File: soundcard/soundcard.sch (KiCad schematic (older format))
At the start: 32 parts, among them U1 74LS590, U10 74HC164, U11 74HC164, U12 74LS86, U2 74LS590, U3 74LS688, U4 74LS109, U5 74LS373, U6 74LS373, U8 74LS138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

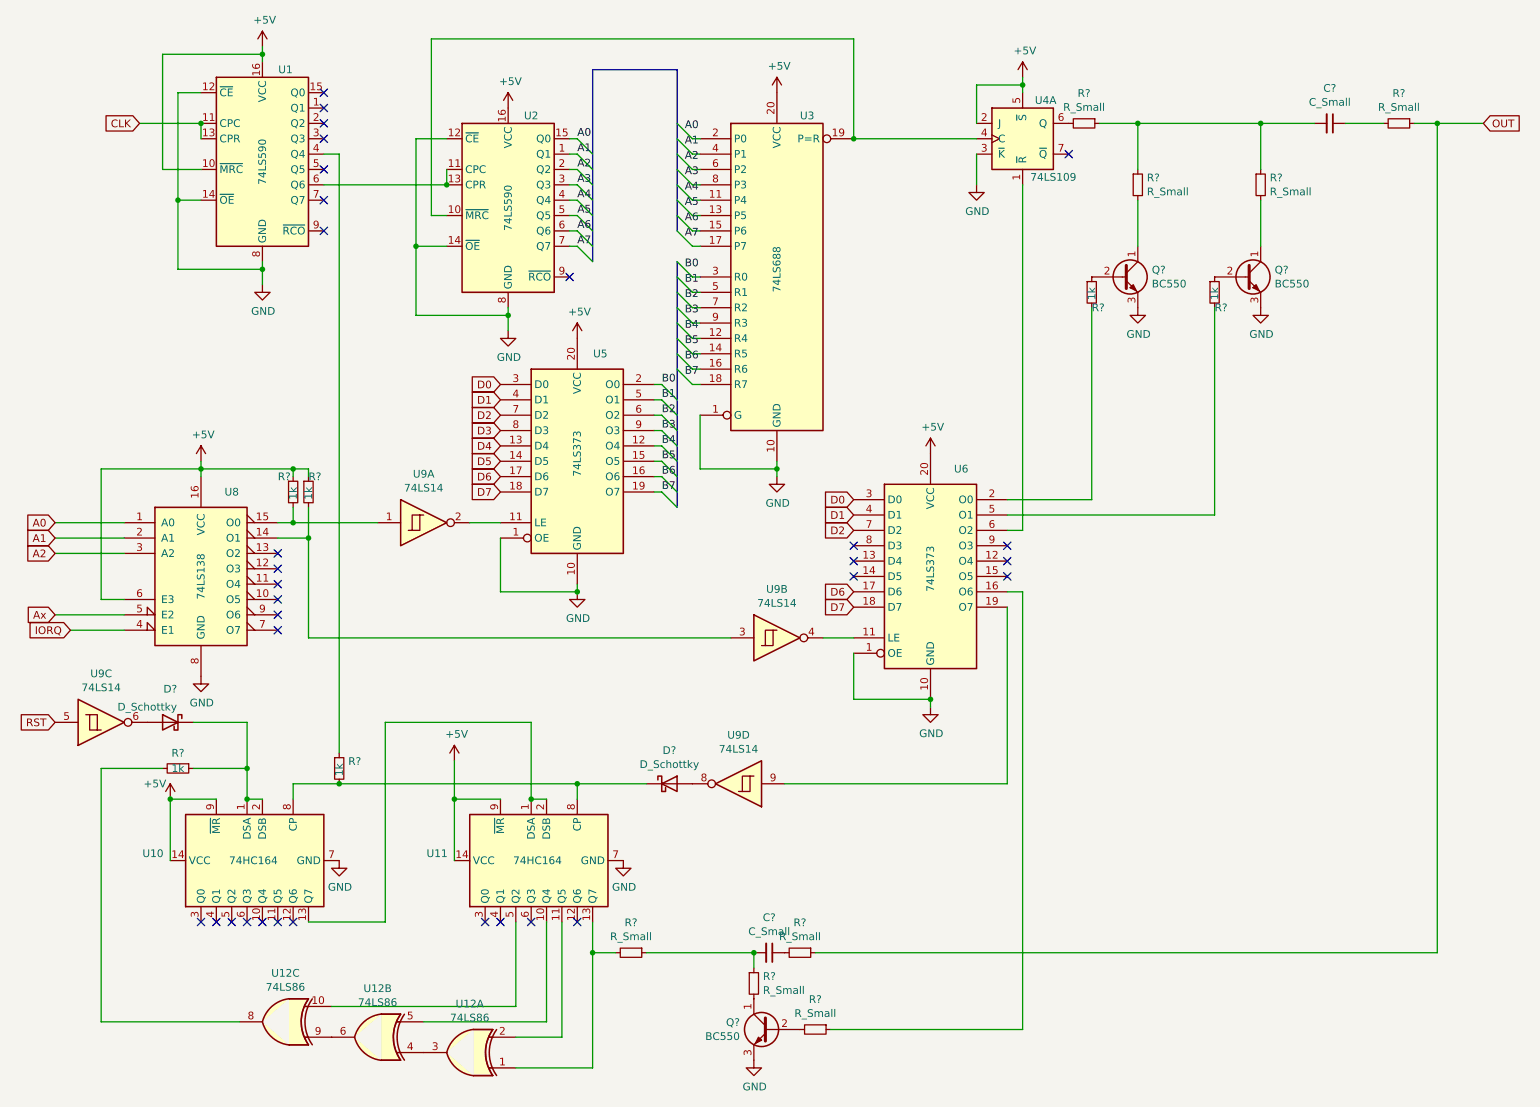
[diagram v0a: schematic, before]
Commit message: stable with ps2 support
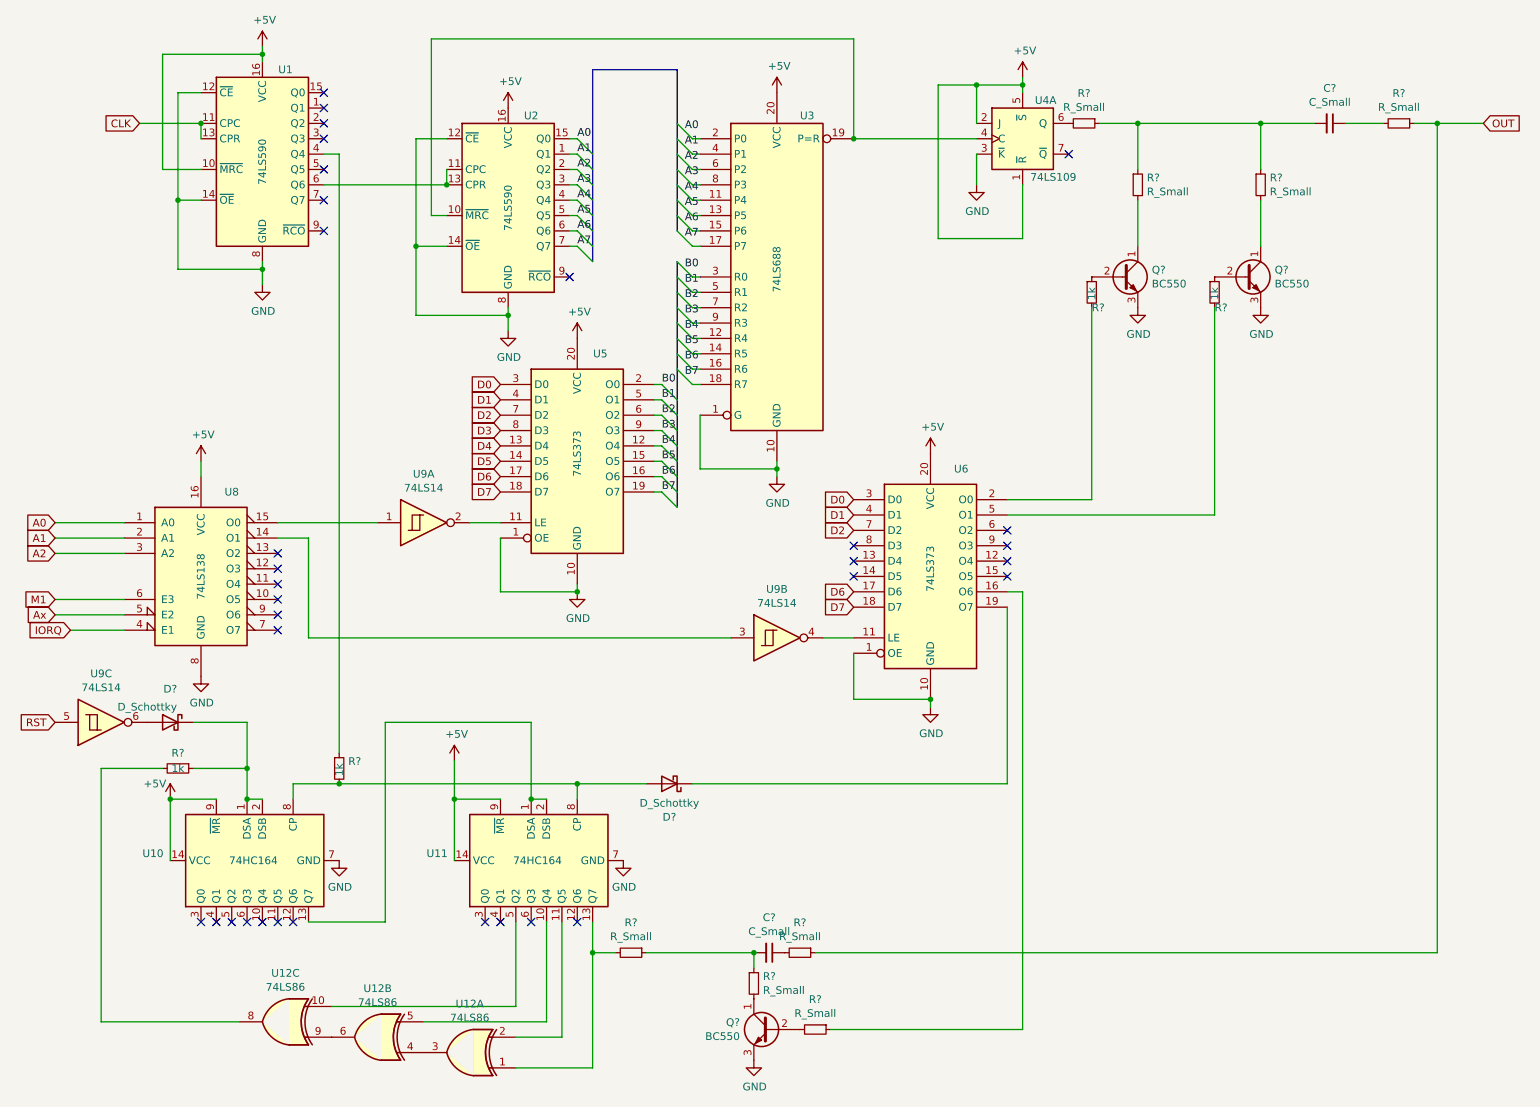
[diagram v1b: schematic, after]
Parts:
- removed R? (x2): 1k, symbol Device:R_Small
- removed unit 4 of U9
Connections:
- net +5V: now also U4.1 (~R); no longer U8.6 (E3)
- net at U6.6 (O2): no longer U4.1 (~R)
- net at U6.19 (O7): now also D?.1 (K)
- net at R?.2, U10.8 (CP), U11.8 (CP): now also D?.2 (A); no longer D?.1 (K)
- new net M1: U8.6 (E3)
- no-connect marks 32 -> 33
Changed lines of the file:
@@
-$EndComp
-$Comp
-L 74xx:74LS373 U6
-U 1 1 628CBCB8
-P 6450 4200
-F 0 "U6" H 6650 4900 50  0000 C CNN
-F 1 "74LS373" V 6450 4250 50  0000 C CNN
-F 2 "" H 6450 4200 50  0001 C CNN
-F 3 "http://www.ti.com/lit/gpn/sn74LS373" H 6450 4200 50  0001 C CNN
-	1    6450 4200
-	1    0    0    -1
 $EndComp
 $Comp
@@
 Wire Wire Line
 	5950 5000 5950 4700
-Connection ~ 6450 5000
 Text GLabel 3650 2950 0    50   Input ~ 0
 D0
@@
 Text GLabel 5950 3900 0    50   Input ~ 0
 D2
-Wire Wire Line
-	1700 3450 1700 3500
-Wire Wire Line
-	1700 3500 1050 3500
-Wire Wire Line
-	1050 3500 1050 4350
-Wire Wire Line
-	1050 4350 1200 4350
-Connection ~ 1700 3500
-Wire Wire Line
-	1700 3500 1700 3550
 Text GLabel 750  4450 0    50   Input ~ 0
 Ax
@@
 Wire Wire Line
 	1200 4550 850  4550
-$Comp
-L Device:R_Small R?
-U 1 1 629251BB
-P 2400 3650
-F 0 "R?" H 2200 3750 50  0000 L CNN
-F 1 "1k" V 2300 3600 50  0000 L CNN
-F 2 "" H 2400 3650 50  0001 C CNN
-F 3 "~" H 2400 3650 50  0001 C CNN
-	1    2400 3650
-	1    0    0    -1
-$EndComp
-$Comp
-L Device:R_Small R?
-U 1 1 629259F8
-P 2300 3650
-F 0 "R?" H 2400 3750 50  0000 L CNN
-F 1 "1k" V 2400 3600 50  0000 L CNN
-F 2 "" H 2300 3650 50  0001 C CNN
-F 3 "~" H 2300 3650 50  0001 C CNN
-	1    2300 3650
-	1    0    0    -1
-$EndComp
-Wire Wire Line
-	2400 3500 2400 3550
-Wire Wire Line
-	2300 3550 2300 3500
 Wire Wire Line
 	5450 3550 5450 3500
@@
 Wire Wire Line
 	2200 3950 2400 3950
-Connection ~ 2300 3500
-Wire Wire Line
-	1700 3500 2300 3500
-Wire Wire Line
-	2300 3500 2400 3500
-Wire Wire Line
-	2400 3750 2400 3950
-Wire Wire Line
-	2300 3750 2300 3850
-Connection ~ 2300 3850
-Wire Wire Line
-	2300 3850 2200 3850
 Wire Wire Line
 	2500 1650 3300 1650
-Wire Wire Line
-	6950 3900 7050 3900
 $Comp
 L Device:R_Small R?
@@
 	9400 1250 9150 1250
 Wire Wire Line
-	7050 1650 7050 3900
-Wire Wire Line
 	7500 3700 7500 2450
 Wire Wire Line
@@
 Connection ~ 7050 1000
 Wire Wire Line
-	2300 3850 2850 3850
-Wire Wire Line
 	2400 3950 2400 4600
 Wire Wire Line
 	2400 4600 5150 4600
-Connection ~ 2400 3950
 $Comp
 L 74xx:74HC164 U10
@@
 NoConn ~ 2200 4450
 NoConn ~ 2200 4550
-$Comp
-L 74xx:74LS14 U9
-U 4 1 62B1065C
-P 5200 5550
-F 0 "U9" H 5200 5233 50  0000 C CNN
-F 1 "74LS14" H 5200 5324 50  0000 C CNN
-F 2 "" H 5200 5550 50  0001 C CNN
-F 3 "http://www.ti.com/lit/gpn/sn74LS14" H 5200 5550 50  0001 C CNN
-	4    5200 5550
-	-1   0    0    1
-$EndComp
 Wire Wire Line
 	6950 4400 6950 5550
-Wire Wire Line
-	6950 5550 5500 5550
 $Comp
 L Device:D_Schottky D?
@@
 F 3 "~" H 4750 5550 50  0001 C CNN
 	1    4750 5550
-	1    0    0    -1
+	-1   0    0    1
 $EndComp
 Wire Wire Line
@@
 Wire Wire Line
 	9750 6650 9750 1250
+Connection ~ 9750 1250
+Wire Wire Line
+	9750 1250 10050 1250
+Wire Wire Line
+	2200 3850 2850 3850
+Wire Wire Line
+	1700 3450 1700 3550
+Text GLabel 750  4350 0    50   Input ~ 0
+M1
+Wire Wire Line
+	750  4350 1200 4350
+Wire Wire Line
+	7050 1650 7050 2000
+Wire Wire Line
+	7050 2000 6500 2000
+Wire Wire Line
+	6500 2000 6500 1000
+Wire Wire Line
+	6500 1000 6750 1000
+Connection ~ 6750 1000
+Connection ~ 6450 5000
+$Comp
+L 74xx:74LS373 U6
+U 1 1 628CBCB8
+P 6450 4200
+F 0 "U6" H 6650 4900 50  0000 C CNN
+F 1 "74LS373" V 6450 4250 50  0000 C CNN
+F 2 "" H 6450 4200 50  0001 C CNN
+F 3 "http://www.ti.com/lit/gpn/sn74LS373" H 6450 4200 50  0001 C CNN
+	1    6450 4200
+	1    0    0    -1
+$EndComp
+NoConn ~ 6950 3900
+Wire Wire Line
+	4900 5550 6950 5550
+Wire Bus Line
+	4800 900  4800 1950
 Wire Bus Line
 	4250 900  4250 2150
 Wire Bus Line
-	4800 900  4800 1950
-Wire Bus Line
 	4800 2150 4800 3750
-Connection ~ 9750 1250
-Wire Wire Line
-	9750 1250 10050 1250
 $EndSCHEMATC
